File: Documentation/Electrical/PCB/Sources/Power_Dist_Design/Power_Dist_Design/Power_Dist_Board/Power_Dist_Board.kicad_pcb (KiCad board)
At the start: 2 copper layers, 150.5 x 84.8 mm, 59 parts, among them J1 Battery Connector, J2 +5V, J3 +5V, J4 +3.3V, J5 +3.3V, J6 GND, J7 GND, M1 Motor_DC, M10 Motor_DC, M2 Motor_DC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

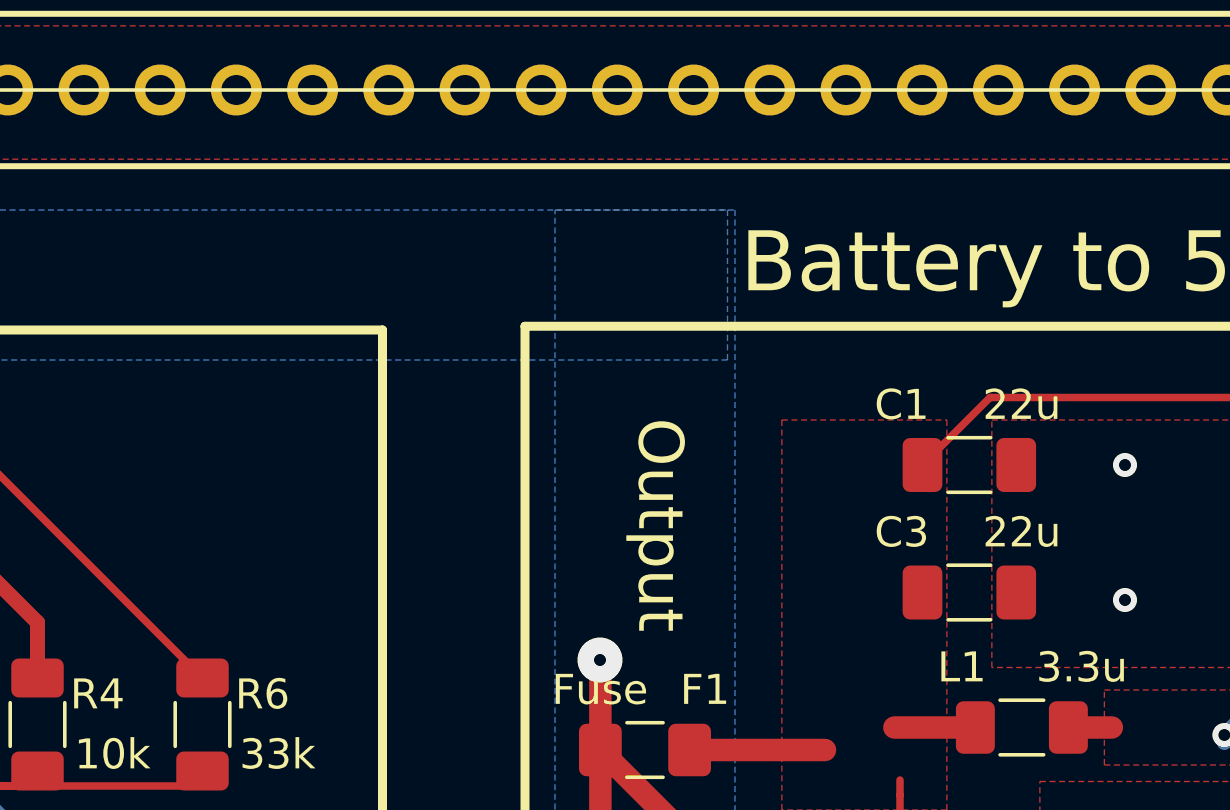
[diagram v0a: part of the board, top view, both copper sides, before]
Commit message: Edited pcb to give better grounding layout
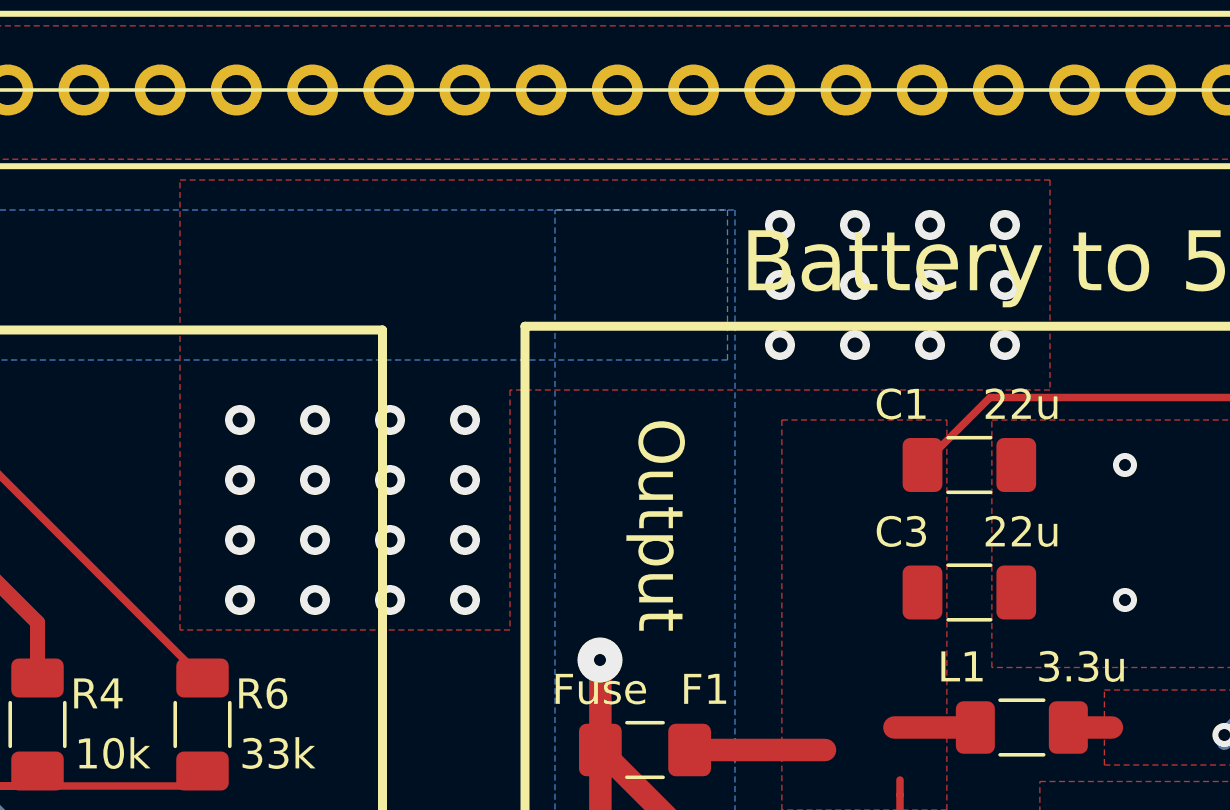
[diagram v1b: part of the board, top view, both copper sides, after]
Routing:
- net GND: vias 18 -> 46
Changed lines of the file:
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@@
   (segment (start 220.5 88.5) (end 222 87) (width 0.5) (layer "F.Cu") (net 2))
   (segment (start 214.5 70) (end 215.314 69.186) (width 0.5) (layer "F.Cu") (net 2))
+  (via (at 151.5 54) (size 1) (drill 0.5) (layers "F.Cu" "B.Cu") (free) (net 2))
+  (via (at 167 49.5) (size 1) (drill 0.5) (layers "F.Cu" "B.Cu") (free) (net 2))
   (via (at 126 58) (size 0.8) (drill 0.4) (layers "F.Cu" "B.Cu") (free) (net 2))
   (via (at 217.5 66.60865) (size 1) (drill 0.4) (layers "F.Cu" "B.Cu") (net 2))
+  (via (at 167 47.5) (size 1) (drill 0.5) (layers "F.Cu" "B.Cu") (free) (net 2))
   (via (at 99 55) (size 1) (drill 0.4) (layers "F.Cu" "B.Cu") (net 2))
   (via (at 126 53.5) (size 0.8) (drill 0.4) (layers "F.Cu" "B.Cu") (free) (net 2))
+  (via (at 149 54) (size 1) (drill 0.5) (layers "F.Cu" "B.Cu") (free) (net 2))
+  (via (at 172 45.5) (size 1) (drill 0.5) (layers "F.Cu" "B.Cu") (free) (net 2))
+  (via (at 154 52) (size 1) (drill 0.5) (layers "F.Cu" "B.Cu") (free) (net 2))
+  (via (at 167 45.5) (size 1) (drill 0.5) (layers "F.Cu" "B.Cu") (free) (net 2))
   (via (at 182.5 58) (size 0.8) (drill 0.4) (layers "F.Cu" "B.Cu") (free) (net 2))
+  (via (at 156.5 58) (size 1) (drill 0.5) (layers "F.Cu" "B.Cu") (free) (net 2))
   (via (at 130 53.5) (size 0.8) (drill 0.4) (layers "F.Cu" "B.Cu") (free) (net 2))
   (via (at 178.5 53.5) (size 0.8) (drill 0.4) (layers "F.Cu" "B.Cu") (free) (net 2))
+  (via (at 174.5 45.5) (size 1) (drill 0.5) (layers "F.Cu" "B.Cu") (free) (net 2))
+  (via (at 169.5 47.5) (size 1) (drill 0.5) (layers "F.Cu" "B.Cu") (free) (net 2))
+  (via (at 174.5 47.5) (size 1) (drill 0.5) (layers "F.Cu" "B.Cu") (free) (net 2))
   (via (at 182.5 53.5) (size 0.8) (drill 0.4) (layers "F.Cu" "B.Cu") (free) (net 2))
+  (via (at 154 54) (size 1) (drill 0.5) (layers "F.Cu" "B.Cu") (free) (net 2))
   (via (at 99 64.3125) (size 1) (drill 0.4) (layers "F.Cu" "B.Cu") (net 2))
+  (via (at 174.5 49.5) (size 1) (drill 0.5) (layers "F.Cu" "B.Cu") (free) (net 2))
+  (via (at 156.5 52) (size 1) (drill 0.5) (layers "F.Cu" "B.Cu") (free) (net 2))
   (via (at 99.5 85) (size 1) (drill 0.4) (layers "F.Cu" "B.Cu") (net 2))
   (via (at 217.5 76.5) (size 1) (drill 0.4) (layers "F.Cu" "B.Cu") (net 2))
+  (via (at 149 52) (size 1) (drill 0.5) (layers "F.Cu" "B.Cu") (free) (net 2))
+  (via (at 169.5 49.5) (size 1) (drill 0.5) (layers "F.Cu" "B.Cu") (free) (net 2))
+  (via (at 149 58) (size 1) (drill 0.5) (layers "F.Cu" "B.Cu") (free) (net 2))
   (via (at 222 87) (size 1) (drill 0.4) (layers "F.Cu" "B.Cu") (net 2))
+  (via (at 172 49.5) (size 1) (drill 0.5) (layers "F.Cu" "B.Cu") (free) (net 2))
+  (via (at 156.5 56) (size 1) (drill 0.5) (layers "F.Cu" "B.Cu") (free) (net 2))
+  (via (at 151.5 56) (size 1) (drill 0.5) (layers "F.Cu" "B.Cu") (free) (net 2))
+  (via (at 149 56) (size 1) (drill 0.5) (layers "F.Cu" "B.Cu") (free) (net 2))
   (via (at 218 45.5) (size 1) (drill 0.4) (layers "F.Cu" "B.Cu") (net 2))
+  (via (at 172 47.5) (size 1) (drill 0.5) (layers "F.Cu" "B.Cu") (free) (net 2))
+  (via (at 151.5 58) (size 1) (drill 0.5) (layers "F.Cu" "B.Cu") (free) (net 2))
   (via (at 99 75) (size 1) (drill 0.4) (layers "F.Cu" "B.Cu") (net 2))
+  (via (at 154 58) (size 1) (drill 0.5) (layers "F.Cu" "B.Cu") (free) (net 2))
+  (via (at 154 56) (size 1) (drill 0.5) (layers "F.Cu" "B.Cu") (free) (net 2))
   (via (at 130 58) (size 0.8) (drill 0.4) (layers "F.Cu" "B.Cu") (free) (net 2))
   (via (at 217.5 56.25) (size 1) (drill 0.4) (layers "F.Cu" "B.Cu") (net 2))
+  (via (at 156.5 54) (size 1) (drill 0.5) (layers "F.Cu" "B.Cu") (free) (net 2))
+  (via (at 151.5 52) (size 1) (drill 0.5) (layers "F.Cu" "B.Cu") (free) (net 2))
+  (via (at 169.5 45.5) (size 1) (drill 0.5) (layers "F.Cu" "B.Cu") (free) (net 2))
   (via (at 99.5 96) (size 1) (drill 0.4) (layers "F.Cu" "B.Cu") (net 2))
   (via (at 178.5 58) (size 0.8) (drill 0.4) (layers "F.Cu" "B.Cu") (free) (net 2))
@@
     )
   )
+  (zone (net 2) (net_name "GND") (layer "F.Cu") (hatch edge 0.5)
+    (priority 2)
+    (connect_pads (clearance 0))
+    (min_thickness 0.25) (filled_areas_thickness no)
+    (fill yes (thermal_gap 0.5) (thermal_bridge_width 0.5))
+    (polygon
+      (pts
+        (xy 147 44)
+        (xy 176 44)
+        (xy 176 51)
+        (xy 158 51)
+        (xy 158 59)
+        (xy 147 59)
+      )
+    )
+  )
   (zone (net 2) (net_name "GND") (layer "F.Cu") (hatch edge 0.508)
     (connect_pads (clearance 0.508))
@@
     (polygon
       (pts
-        (xy 225 26)
-        (xy 225 24)
-        (xy 87 24)
-        (xy 87 26)
+        (xy 225 25.5)
+        (xy 225 23.5)
+        (xy 139.5 23.5)
+        (xy 139.5 25.5)
+      )
+    )
+  )
+  (zone (net 0) (net_name "") (layers "B.Cu" "Eco1.User") (hatch edge 0.5)
+    (connect_pads (clearance 0))
+    (min_thickness 0.25) (filled_areas_thickness no)
+    (keepout (tracks allowed) (vias allowed) (pads allowed) (copperpour not_allowed) (footprints allowed))
+    (fill (thermal_gap 0.5) (thermal_bridge_width 0.5))
+    (polygon
+      (pts
+        (xy 139.5 25.5)
+        (xy 141.5 25.5)
+        (xy 141.5 22.5)
+        (xy 139.5 22.5)
       )
     )
@@
       )
     )
+  )
+  (zone (net 0) (net_name "") (layers "B.Cu" "Eco1.User") (hatch edge 0.5)
+    (connect_pads (clearance 0))
+    (min_thickness 0.25) (filled_areas_thickness no)
+    (keepout (tracks allowed) (vias allowed) (pads allowed) (copperpour not_allowed) (footprints allowed))
+    (fill (thermal_gap 0.5) (thermal_bridge_width 0.5))
+    (polygon
+      (pts
+        (xy 141.500154 24.473685)
+        (xy 141.500154 22.473685)
+        (xy 86.000154 22.473685)
+        (xy 86.000154 24.473685)
+      )
+    )

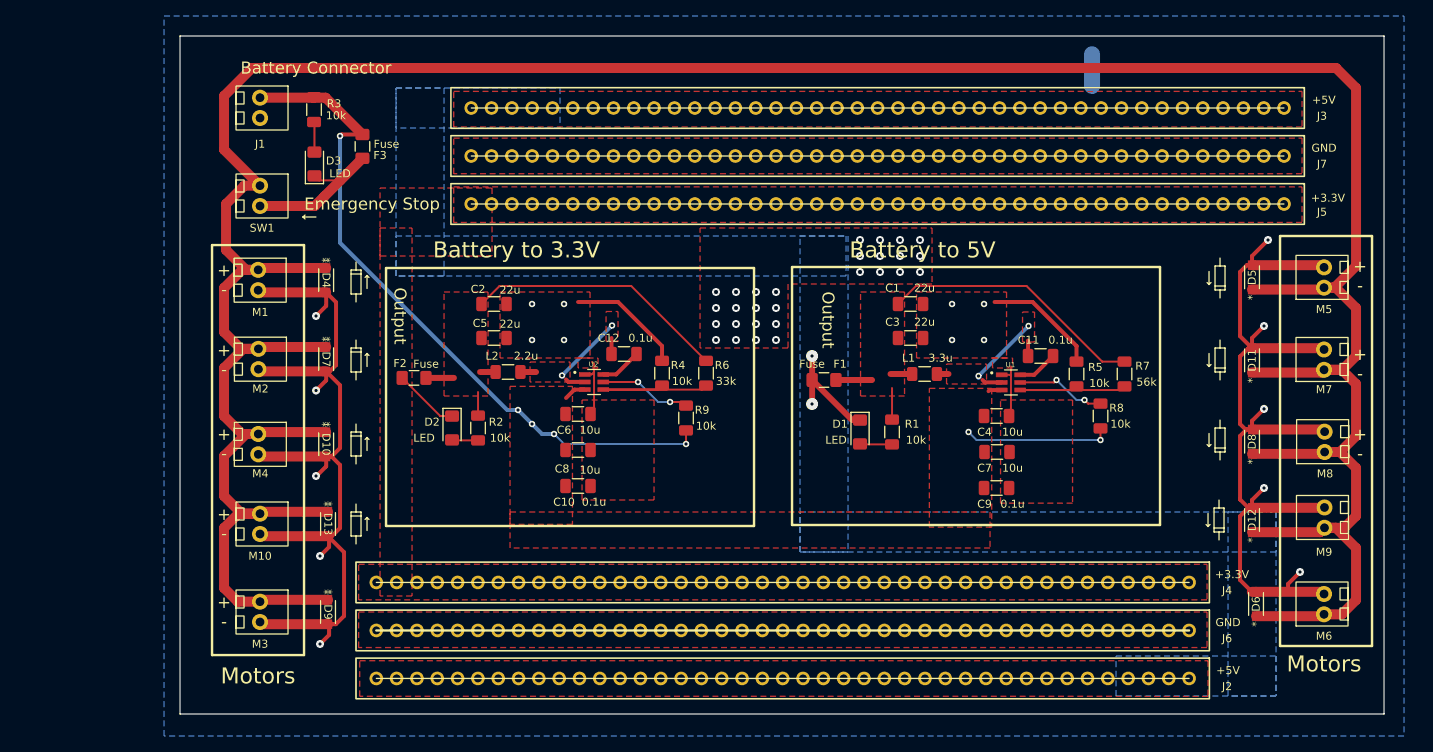
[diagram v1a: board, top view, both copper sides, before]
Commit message: Changed ground plane and added jumpers to motor-ground and ground connection
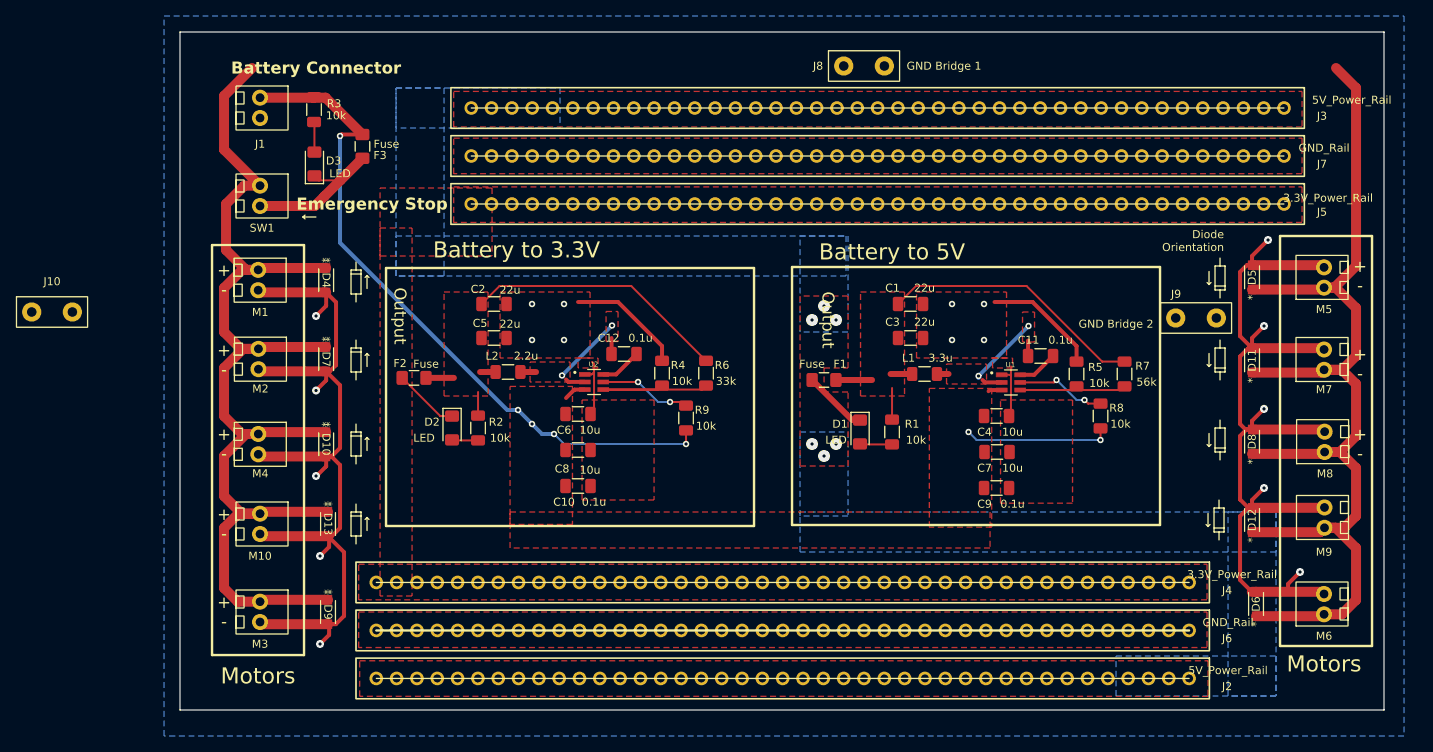
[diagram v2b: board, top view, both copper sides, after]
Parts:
- added J10: GND_Bridge_3, Power_Dist:GND_Bridge, F.Cu at (66.0, 54.5)
- added J8: GND Bridge 1, Power_Dist:GND_Bridge, F.Cu at (167.5, 23.8)
- added J9: GND Bridge 2, Power_Dist:GND_Bridge, F.Cu at (209.0, 55.2)
- J2, J3: value +5V -> 5V_Power_Rail
- J4, J5: value +3.3V -> 3.3V_Power_Rail
- J6, J7: value GND -> GND_Rail
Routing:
- net +12V: track 416.2 -> 280.7 mm
- net +5V: track 14.1 -> 8.06 mm, vias 2 -> 6
- net GND: track 264.3 -> 260.3 mm, vias 46 -> 18
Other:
- board text added: "Diode Orientation"

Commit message: Finalized pcb
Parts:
- J2, J3: value 5V_Power_Rail -> +5V
- J4, J5: value 3.3V_Power_Rail -> +3.3V
- J6, J7: value GND_Rail -> GND
- J8: value GND Bridge 1 -> GND_Bridge_1
- J9: value GND Bridge 2 -> GND_Bridge_2
- L1, L2: footprint Resistor_SMD:R_1206_3216Metric_Pad1.30x1.75mm_HandSolder -> L_TDK_SPM6530:IND_SPM6530_TDK
- moved J10 52.5 mm to (110.5, 82.5)
- moved L2 1.80 mm to (121.5, 63.0)
- moved L1 1.73 mm to (173.5, 63.0)
- moved C6 0.50 mm to (131.8, 67.8)
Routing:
- net +12V: track 280.7 -> 418.7 mm
- net GND: track 260.3 -> 251.4 mm
- net /sw1: track 15.1 -> 14.1 mm
- net /sw2: track 15.2 -> 16.2 mm
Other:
- board text added: "GND Bridge 2"
- board text added: "GND Bridge 3"

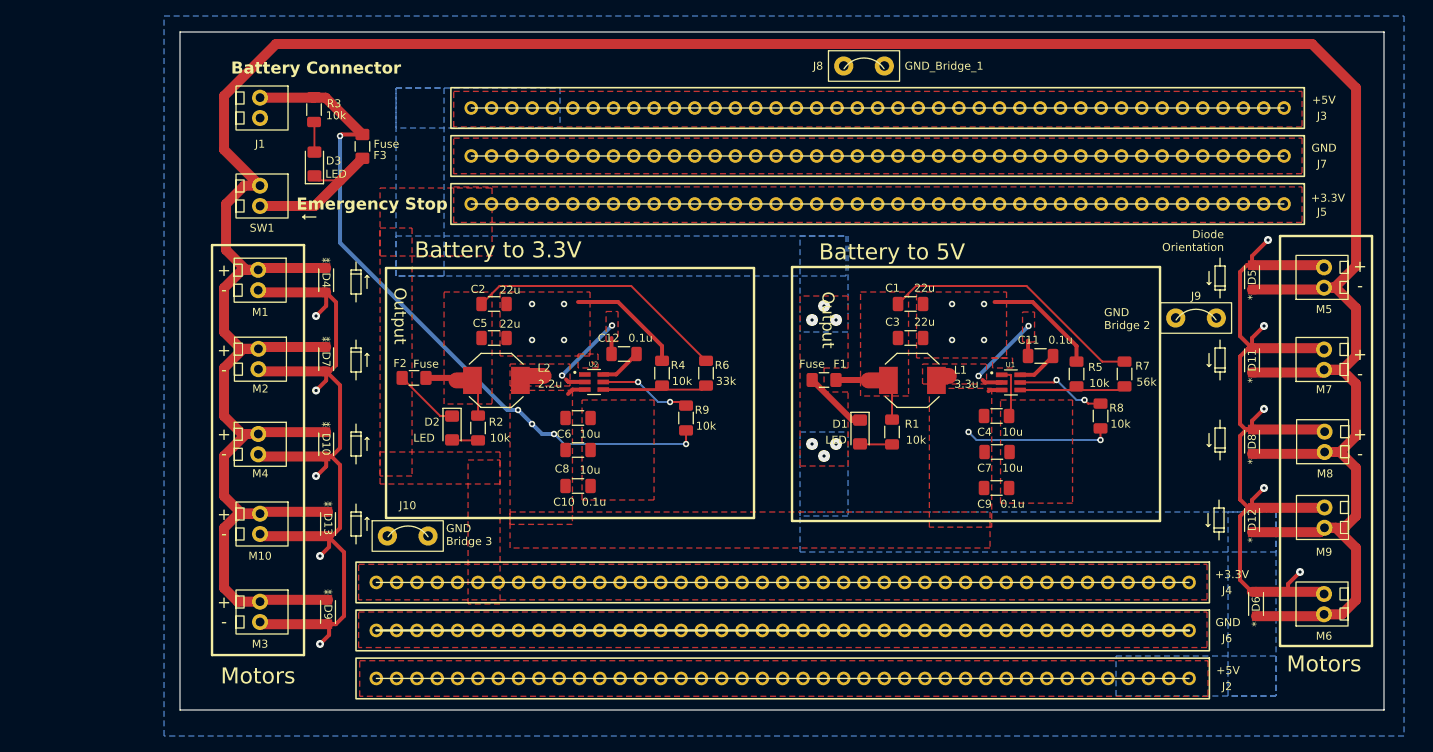
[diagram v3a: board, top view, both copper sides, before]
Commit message: Added screw holes to board and generated gerber file
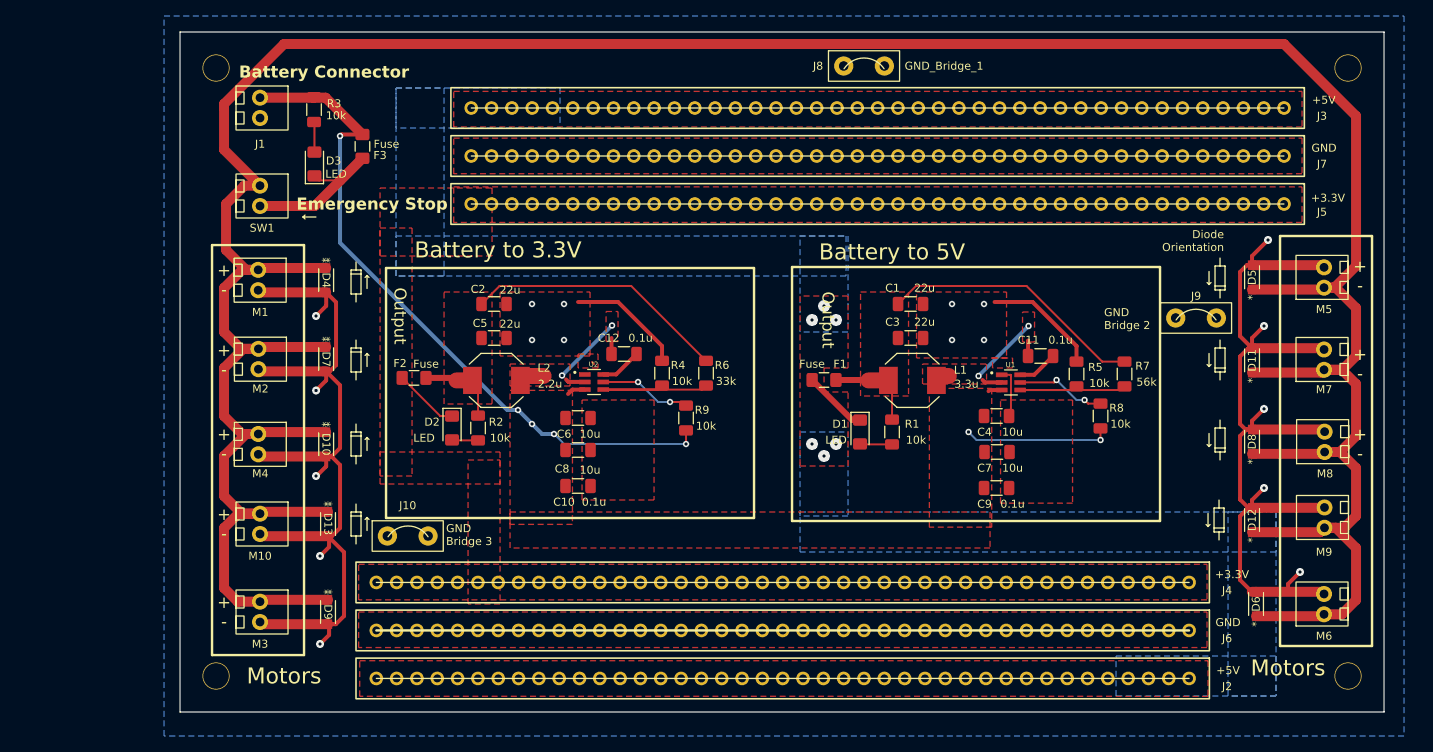
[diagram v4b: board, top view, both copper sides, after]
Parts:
- added REF**: MountingHole_3.2mm_M3_DIN965, MountingHole:MountingHole_3.2mm_M3_DIN965, F.Cu at (228.0, 100.0)
- added REF**: MountingHole_3.2mm_M3_DIN965, MountingHole:MountingHole_3.2mm_M3_DIN965, F.Cu at (86.5, 100.0)
- added REF**: MountingHole_3.2mm_M3_DIN965, MountingHole:MountingHole_3.2mm_M3_DIN965, F.Cu at (228.0, 24.0)
- added REF**: MountingHole_3.2mm_M3_DIN965, MountingHole:MountingHole_3.2mm_M3_DIN965, F.Cu at (86.5, 24.0)
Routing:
- net +12V: track 418.7 -> 416.1 mm
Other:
- board size 150.5 x 84.8 mm -> 150.5 x 85 mm
